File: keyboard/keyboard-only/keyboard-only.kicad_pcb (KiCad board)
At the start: 2 copper layers, 252.7 x 94 mm, 203 parts, among them J1 USB_C_Receptacle_USB2.0, SW1 SW_PUSH, SW10 SW_PUSH, SW11 SW_PUSH, SW12 SW_PUSH, SW13 SW_PUSH, SW14 SW_PUSH, SW15 SW_PUSH, SW16 SW_PUSH, SW17 SW_PUSH, SW18 SW_PUSH, SW19 SW_PUSH, SW2 SW_PUSH, SW20 SW_PUSH, SW21 SW_PUSH, SW22 SW_PUSH, SW23 SW_PUSH, SW24 SW_PUSH, SW25 SW_PUSH, SW26 SW_PUSH, SW27 SW_PUSH, SW28 SW_PUSH, SW29 SW_PUSH, SW3 SW_PUSH, SW30 SW_PUSH, SW31 SW_PUSH, SW32 SW_PUSH, SW33 SW_PUSH, SW34 SW_PUSH, SW35 SW_PUSH, SW36 SW_PUSH, SW37 SW_PUSH, SW38 SW_PUSH, SW39 SW_PUSH, SW4 SW_PUSH, SW40 SW_PUSH, SW41 SW_PUSH, SW42 SW_PUSH, SW43 SW_PUSH, SW44 SW_PUSH, SW45 SW_PUSH, SW46 SW_PUSH, SW47 SW_PUSH, SW48 SW_PUSH, SW49 SW_PUSH, SW5 SW_PUSH, SW50 SW_PUSH, SW51 SW_PUSH, SW52 SW_PUSH, SW53 SW_PUSH, SW54 SW_PUSH, SW55 SW_PUSH, SW56 SW_PUSH, SW57 SW_PUSH, SW58 SW_PUSH, SW59 SW_PUSH, SW6 SW_PUSH, SW60 SW_PUSH, SW7 SW_PUSH, SW8 SW_PUSH, SW9 SW_PUSH, U1 ATmega16U4-AU, Y1 16MHz

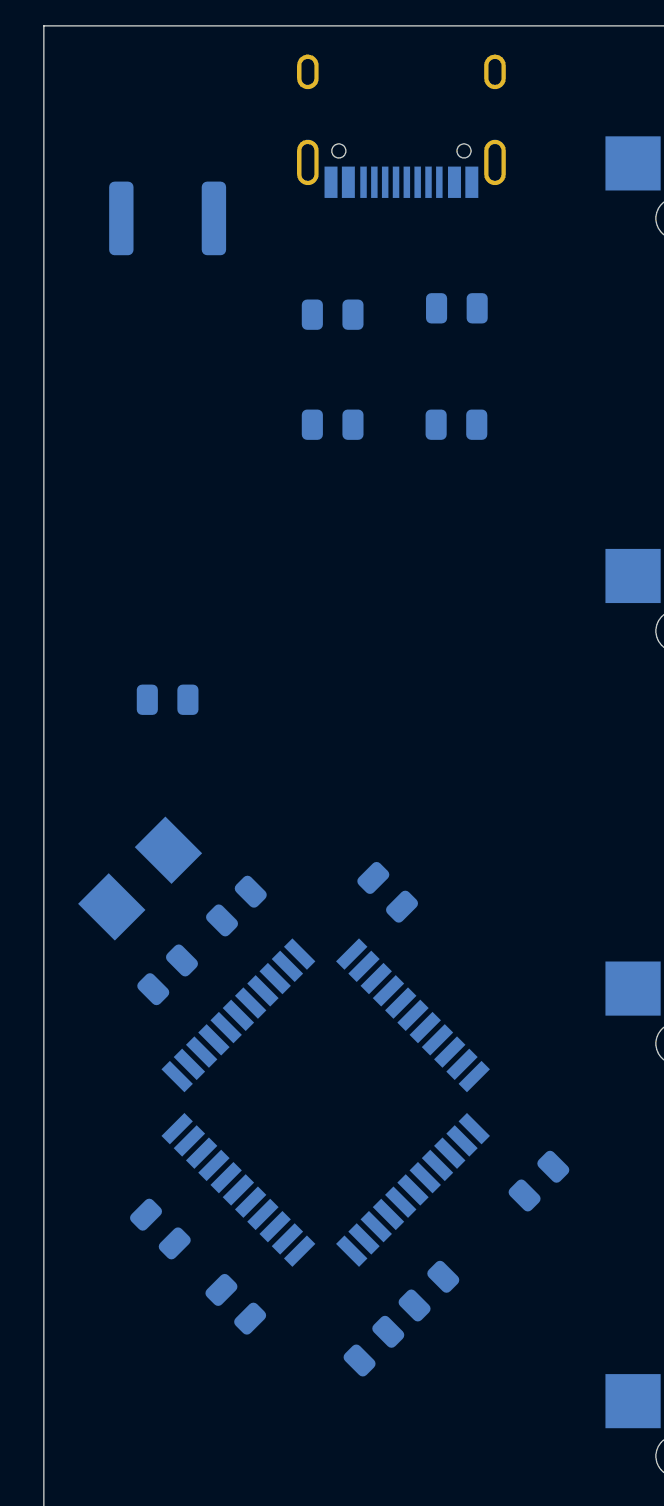
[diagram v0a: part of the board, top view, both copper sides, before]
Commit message: Setup USB differential pair
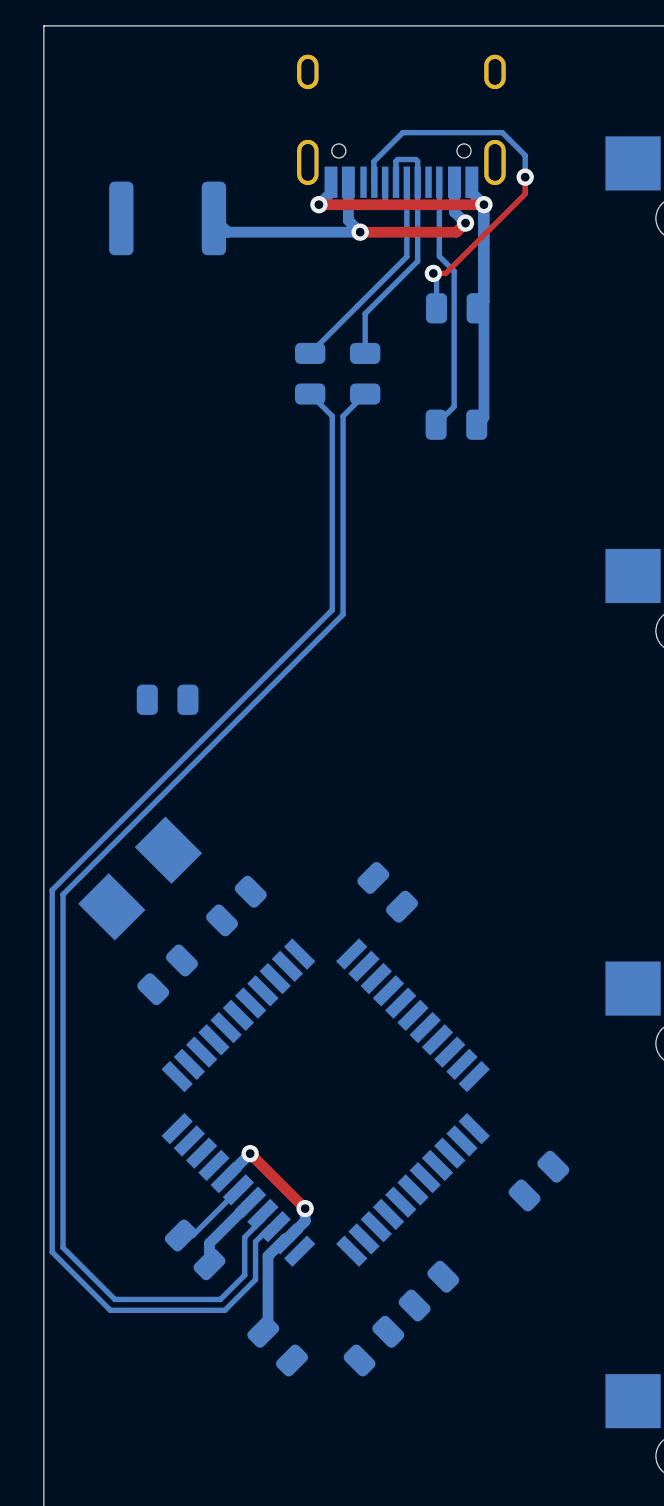
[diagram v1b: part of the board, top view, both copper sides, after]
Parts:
- moved C1 7.65 mm to (32.4, 83.2)
- moved C5 3.14 mm to (28.6, 78.7)
- moved R8 2.92 mm to (33.9, 38.3), turned to 90 degrees
- moved R7 2.79 mm to (36.4, 38.3), turned to 90 degrees
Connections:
- R7 pad 1: N$9 (its old number) -> RD+
- R8 pad 1: N$10 (its old number) -> RD-
- U1 pad 3: N$10 (its old number) -> RD-
- U1 pad 4: N$9 (its old number) -> RD+
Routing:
- net RD-: track 0.00 -> 59.4 mm
- net RD+: track 0.00 -> 58.2 mm
- net GND: track 0.00 -> 29.0 mm, vias 0 -> 2
- net VBUS: track 0.00 -> 28.4 mm, vias 0 -> 4
- net N$1: track 0.00 -> 18.1 mm, vias 0 -> 2
- net D-: track 0.00 -> 12.8 mm
- net D+: track 0.00 -> 11.9 mm
- net N$2: track 0.00 -> 11.8 mm
- net N$9: track 0.00 -> 3.53 mm

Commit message: Begin matrix wiring
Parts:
- moved R6 3.17 mm to (24.8, 55.2)
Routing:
- net GND: track 29.0 -> 60.2 mm
- net VCC: track 0.00 -> 13.1 mm
- net N$11: track 0.00 -> 8.96 mm
- net N$12: track 0.00 -> 8.21 mm
- net N$10: track 0.00 -> 4.05 mm
- net N$131: track 0.00 -> 4.04 mm
- net N$121: track 0.00 -> 4.04 mm
- net N$59: track 0.00 -> 4.04 mm
- net N$49: track 0.00 -> 4.04 mm
- net N$35: track 0.00 -> 4.04 mm
- net N$25: track 0.00 -> 4.04 mm
- net N$97: track 0.00 -> 4.04 mm
- net N$83: track 0.00 -> 4.04 mm
- net N$73: track 0.00 -> 4.04 mm
- net N$115: track 0.00 -> 4.04 mm
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
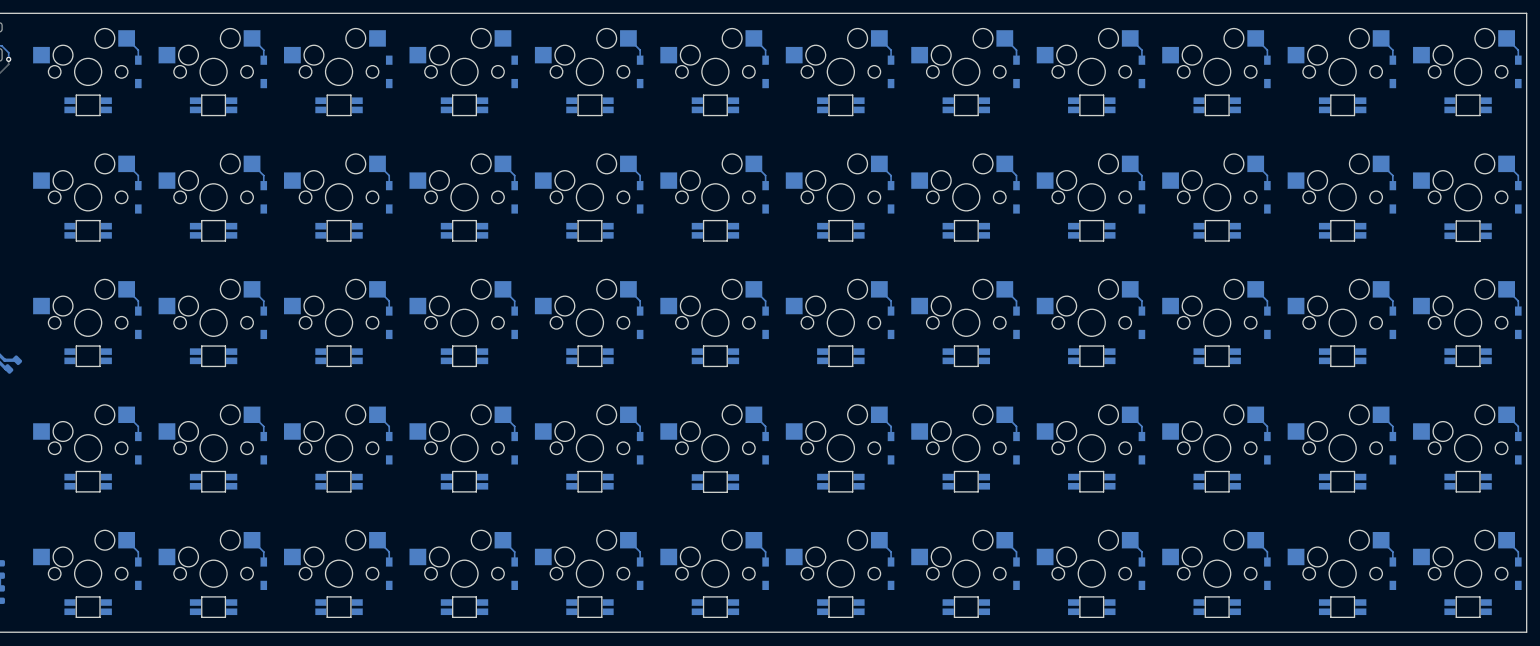
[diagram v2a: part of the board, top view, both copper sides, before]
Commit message: Add LED column wiring
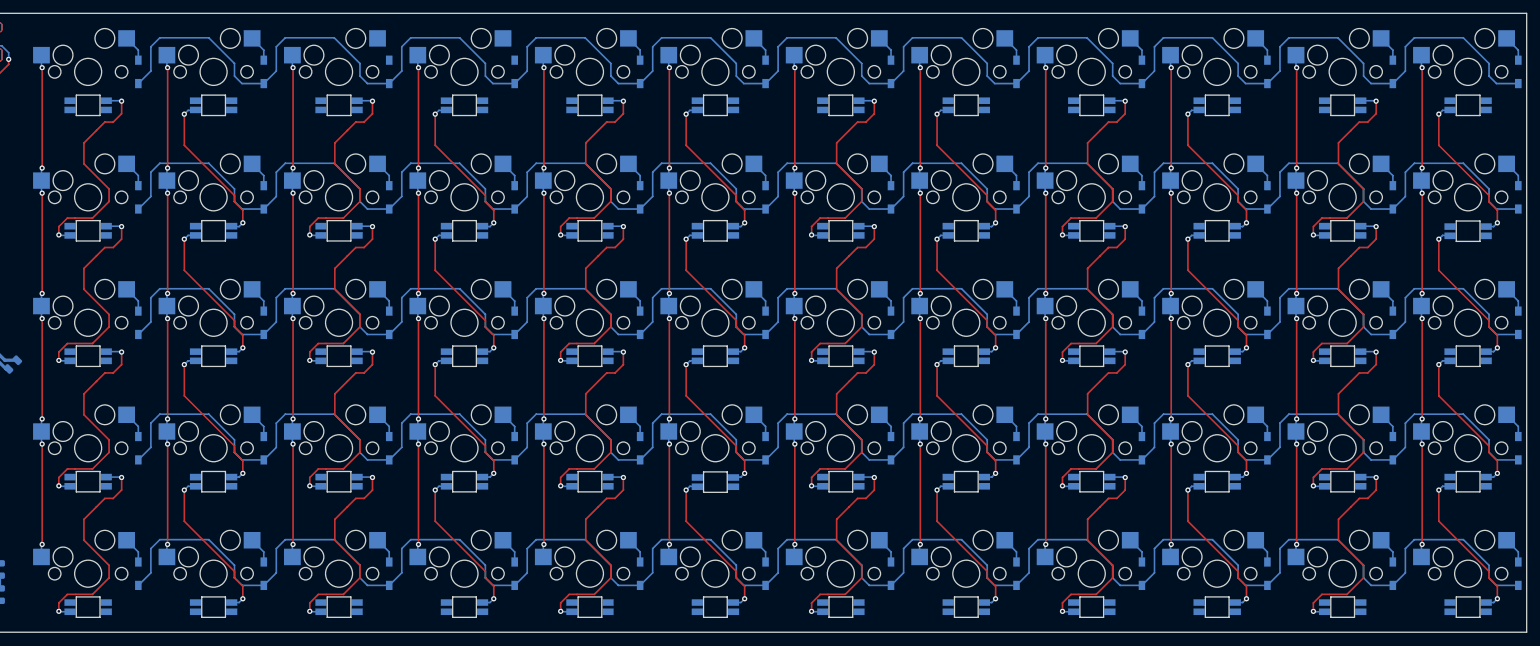
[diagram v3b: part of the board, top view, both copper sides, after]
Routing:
- net ROW4: track 0.00 -> 308.8 mm
- net ROW3: track 0.00 -> 308.8 mm
- net ROW1: track 0.00 -> 308.8 mm
- net ROW0: track 0.00 -> 308.8 mm
- net ROW2: track 0.00 -> 308.8 mm
- net COL0: track 0.00 -> 75.5 mm, vias 0 -> 8
- net COL11: track 0.00 -> 75.5 mm, vias 0 -> 8
- net COL9: track 0.00 -> 75.4 mm, vias 0 -> 8
- net COL8: track 0.00 -> 75.4 mm, vias 0 -> 8
- net COL7: track 0.00 -> 75.4 mm, vias 0 -> 8
- net COL6: track 0.00 -> 75.4 mm, vias 0 -> 8
- net COL5: track 0.00 -> 75.4 mm, vias 0 -> 8
- net COL4: track 0.00 -> 75.4 mm, vias 0 -> 8
- net COL3: track 0.00 -> 75.4 mm, vias 0 -> 8
- net COL2: track 0.00 -> 75.4 mm, vias 0 -> 8
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
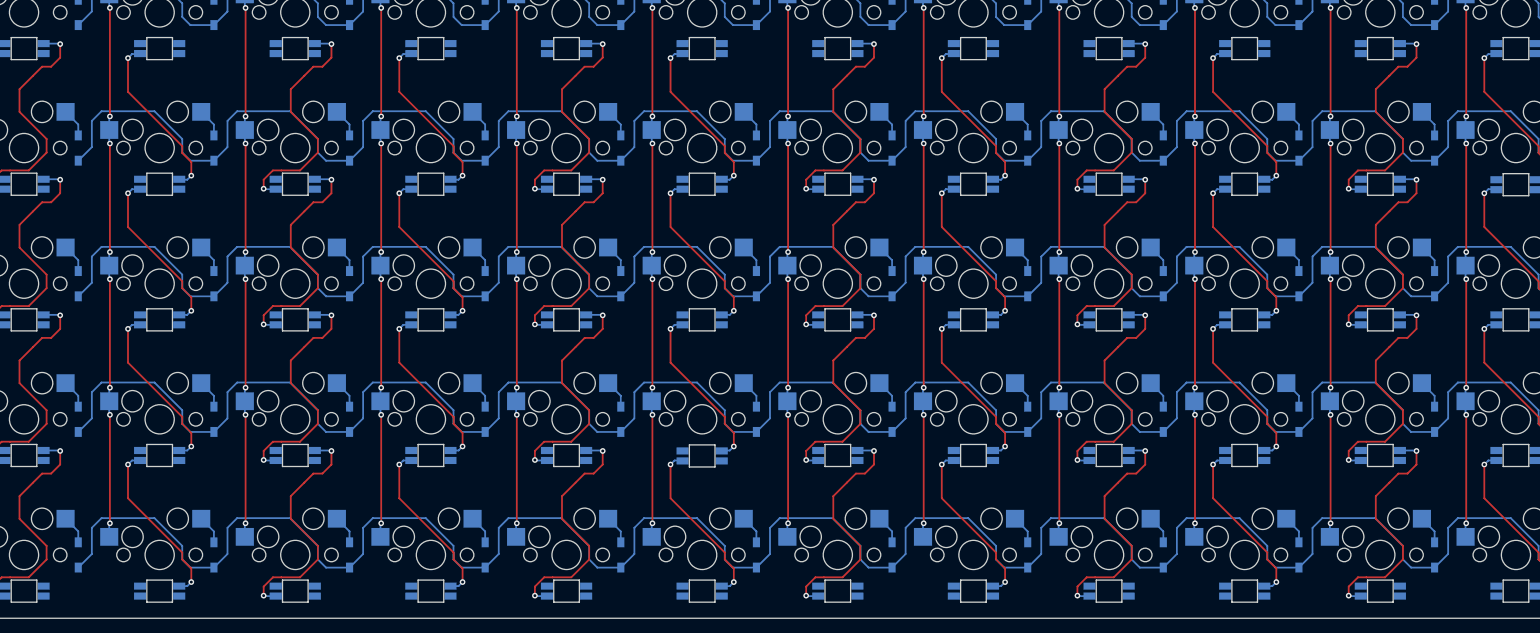
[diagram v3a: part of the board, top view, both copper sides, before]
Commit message: Complete LED data wiring
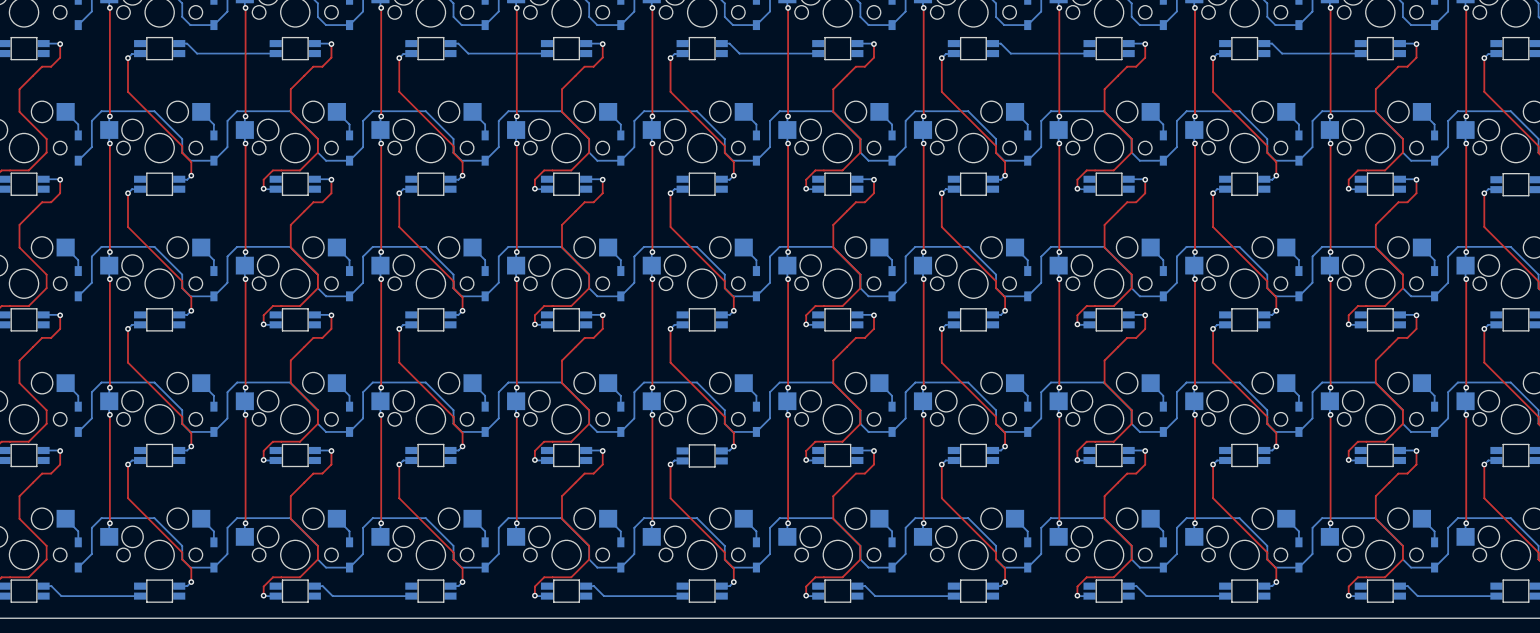
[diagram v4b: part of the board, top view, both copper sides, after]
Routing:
- net N$94: track 0.00 -> 14.1 mm
- net N$74: track 0.00 -> 14.1 mm
- net N$54: track 0.00 -> 14.1 mm
- net N$124: track 0.00 -> 14.1 mm
- net N$104: track 0.00 -> 14.1 mm
- net N$24: track 0.00 -> 14.1 mm
- net N$44: track 0.00 -> 14.1 mm
- net N$34: track 0.00 -> 14.1 mm
- net N$84: track 0.00 -> 14.1 mm
- net N$64: track 0.00 -> 14.1 mm
- net N$114: track 0.00 -> 14.1 mm
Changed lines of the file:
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@@
     (thickness 1.6)
     (drawings 4)
-    (tracks 1594)
+    (tracks 1627)
     (zones 0)
     (modules 203)
@@
   (gr_line (start 274.32 22.225) (end 274.32 116.205) (layer Edge.Cuts) (width 0.05))
   (gr_line (start 21.59 22.225) (end 274.32 22.225) (layer Edge.Cuts) (width 0.05))
+  (segment (start 230.08 35.495) (end 231.18 35.495) (width 0.25) (layer B.Cu) (net 112))
+  (segment (start 231.18 35.495) (end 232.58 36.895) (width 0.25) (layer B.Cu) (net 112))
+  (segment (start 232.58 36.895) (end 243.63 36.895) (width 0.25) (layer B.Cu) (net 112))
+  (segment (start 191.98 35.495) (end 193.08 35.495) (width 0.25) (layer B.Cu) (net 46))
+  (segment (start 193.08 35.495) (end 194.48 36.895) (width 0.25) (layer B.Cu) (net 46))
+  (segment (start 194.48 36.895) (end 205.53 36.895) (width 0.25) (layer B.Cu) (net 46))
+  (segment (start 153.88 35.495) (end 154.98 35.495) (width 0.25) (layer B.Cu) (net 93))
+  (segment (start 154.98 35.495) (end 156.38 36.895) (width 0.25) (layer B.Cu) (net 93))
+  (segment (start 156.38 36.895) (end 167.43 36.895) (width 0.25) (layer B.Cu) (net 93))
+  (segment (start 115.78 35.495) (end 116.88 35.495) (width 0.25) (layer B.Cu) (net 83))
+  (segment (start 116.88 35.495) (end 118.28 36.895) (width 0.25) (layer B.Cu) (net 83))
+  (segment (start 118.28 36.895) (end 129.33 36.895) (width 0.25) (layer B.Cu) (net 83))
+  (segment (start 77.68 35.495) (end 78.78 35.495) (width 0.25) (layer B.Cu) (net 132))
+  (segment (start 78.78 35.495) (end 80.18 36.895) (width 0.25) (layer B.Cu) (net 132))
+  (segment (start 80.18 36.895) (end 91.23 36.895) (width 0.25) (layer B.Cu) (net 132))
+  (segment (start 249.13 111.695) (end 250.23 111.695) (width 0.25) (layer B.Cu) (net 117))
+  (segment (start 250.23 111.695) (end 251.63 113.095) (width 0.25) (layer B.Cu) (net 117))
+  (segment (start 251.63 113.095) (end 262.68 113.095) (width 0.25) (layer B.Cu) (net 117))
+  (segment (start 211.03 111.695) (end 212.13 111.695) (width 0.25) (layer B.Cu) (net 107))
+  (segment (start 212.13 111.695) (end 213.53 113.095) (width 0.25) (layer B.Cu) (net 107))
+  (segment (start 213.53 113.095) (end 224.58 113.095) (width 0.25) (layer B.Cu) (net 107))
+  (segment (start 172.93 111.695) (end 174.03 111.695) (width 0.25) (layer B.Cu) (net 41))
+  (segment (start 174.03 111.695) (end 175.43 113.095) (width 0.25) (layer B.Cu) (net 41))
+  (segment (start 175.43 113.095) (end 186.48 113.095) (width 0.25) (layer B.Cu) (net 41))
+  (segment (start 134.83 111.695) (end 135.93 111.695) (width 0.25) (layer B.Cu) (net 88))
+  (segment (start 135.93 111.695) (end 137.33 113.095) (width 0.25) (layer B.Cu) (net 88))
+  (segment (start 137.33 113.095) (end 148.38 113.095) (width 0.25) (layer B.Cu) (net 88))
+  (segment (start 96.73 111.695) (end 97.83 111.695) (width 0.25) (layer B.Cu) (net 21))
+  (segment (start 97.83 111.695) (end 99.23 113.095) (width 0.25) (layer B.Cu) (net 21))
+  (segment (start 99.23 113.095) (end 110.28 113.095) (width 0.25) (layer B.Cu) (net 21))
   (via (at 60.96 35.56) (size 0.8) (drill 0.4) (layers F.Cu B.Cu) (net 11))
   (segment (start 59.055 48.895) (end 55.245 45.085) (width 0.25) (layer F.Cu) (net 11))
@@
   (segment (start 139.7 27.813) (end 137.922 26.035) (width 0.25) (layer B.Cu) (net 72))
   (segment (start 139.7 29.34) (end 139.7 27.813) (width 0.25) (layer B.Cu) (net 72))
+  (segment (start 61.13 113.095) (end 72.18 113.095) (width 0.25) (layer B.Cu) (net 73))
+  (segment (start 59.73 111.695) (end 61.13 113.095) (width 0.25) (layer B.Cu) (net 73))
+  (segment (start 58.63 111.695) (end 59.73 111.695) (width 0.25) (layer B.Cu) (net 73))
   (segment (start 196.85 27.813) (end 195.072 26.035) (width 0.25) (layer B.Cu) (net 74))
   (segment (start 196.85 29.34) (end 196.85 27.813) (width 0.25) (layer B.Cu) (net 74))

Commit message: Wire columns
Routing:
- net COL11: track 75.5 -> 340.6 mm, vias 8 -> 11
- net COL10: track 75.4 -> 281.2 mm, vias 8 -> 9
- net COL8: track 75.4 -> 278.8 mm, vias 8 -> 11
- net COL9: track 75.4 -> 264.3 mm, vias 8 -> 9
- net COL7: track 75.4 -> 257.8 mm, vias 8 -> 11
- net COL6: track 75.4 -> 236.7 mm, vias 8 -> 11
- net COL5: track 75.4 -> 184.0 mm, vias 8 -> 9
- net COL4: track 75.4 -> 165.0 mm, vias 8 -> 9
- net COL3: track 75.4 -> 146.1 mm, vias 8 -> 9
- net COL2: track 75.4 -> 127.5 mm, vias 8 -> 9
- net COL1: track 75.4 -> 108.7 mm, vias 8 -> 9
- net COL0: track 75.5 -> 89.7 mm

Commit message: Wire all the things even if not that pretty
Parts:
- moved R6 10.3 mm to (34.7, 57.9)
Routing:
- net VCC: track 13.1 -> 1376.0 mm, vias 0 -> 11
- net GND: track 60.2 -> 1384.4 mm, vias 2 -> 10
- net ROW4: track 308.8 -> 378.1 mm, vias 0 -> 2
- net ROW0: track 308.8 -> 363.4 mm, vias 0 -> 4
- net ROW3: track 308.8 -> 361.9 mm, vias 0 -> 2
- net VBUS: track 28.4 -> 76.7 mm
- net N$6: track 0.00 -> 42.5 mm, vias 0 -> 2
- net N$14: track 0.00 -> 40.5 mm, vias 0 -> 2
- net ROW2: track 308.8 -> 345.0 mm, vias 0 -> 2
- net ROW1: track 308.8 -> 343.8 mm, vias 0 -> 2
- net N$4: track 0.00 -> 32.5 mm, vias 0 -> 2
- net N$8: track 0.00 -> 30.7 mm, vias 0 -> 4

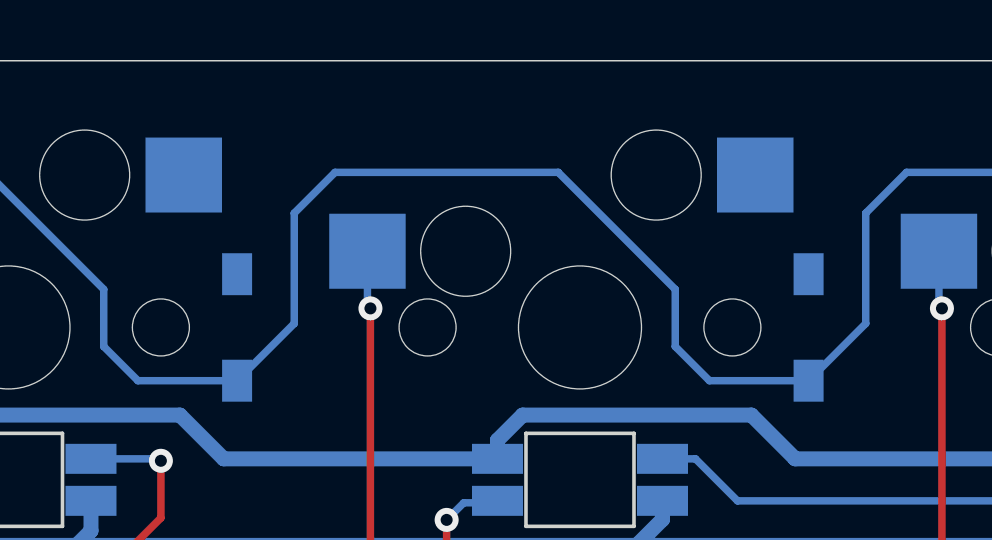
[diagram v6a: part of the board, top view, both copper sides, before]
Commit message: Fix missing wires
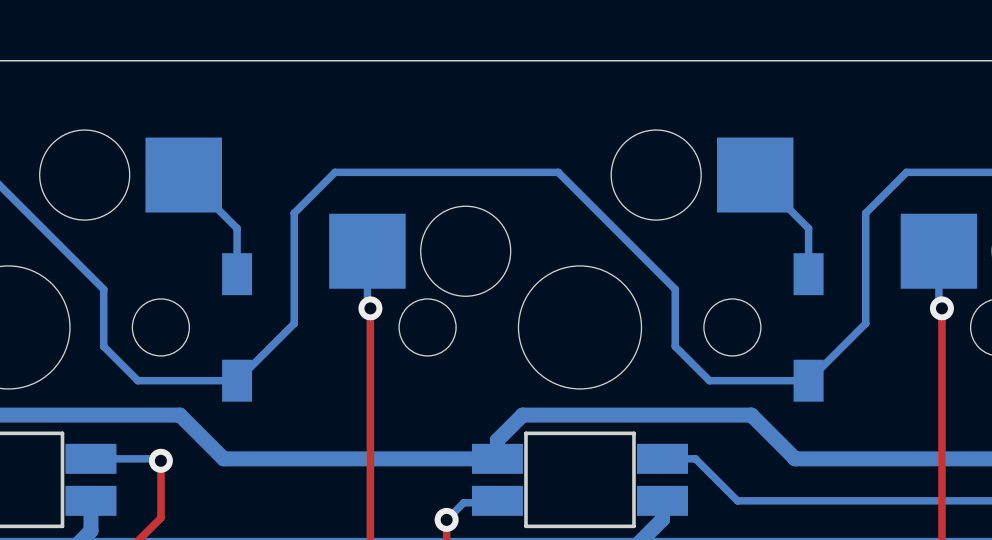
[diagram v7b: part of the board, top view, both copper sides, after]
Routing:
- net N$19: track 0.00 -> 4.04 mm
- net N$17: track 0.00 -> 4.04 mm
